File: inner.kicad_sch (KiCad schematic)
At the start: 5 parts, among them J1 FFC 10x1 0.5mm, J2 USB_A, J3 OLED, J4 Encoder

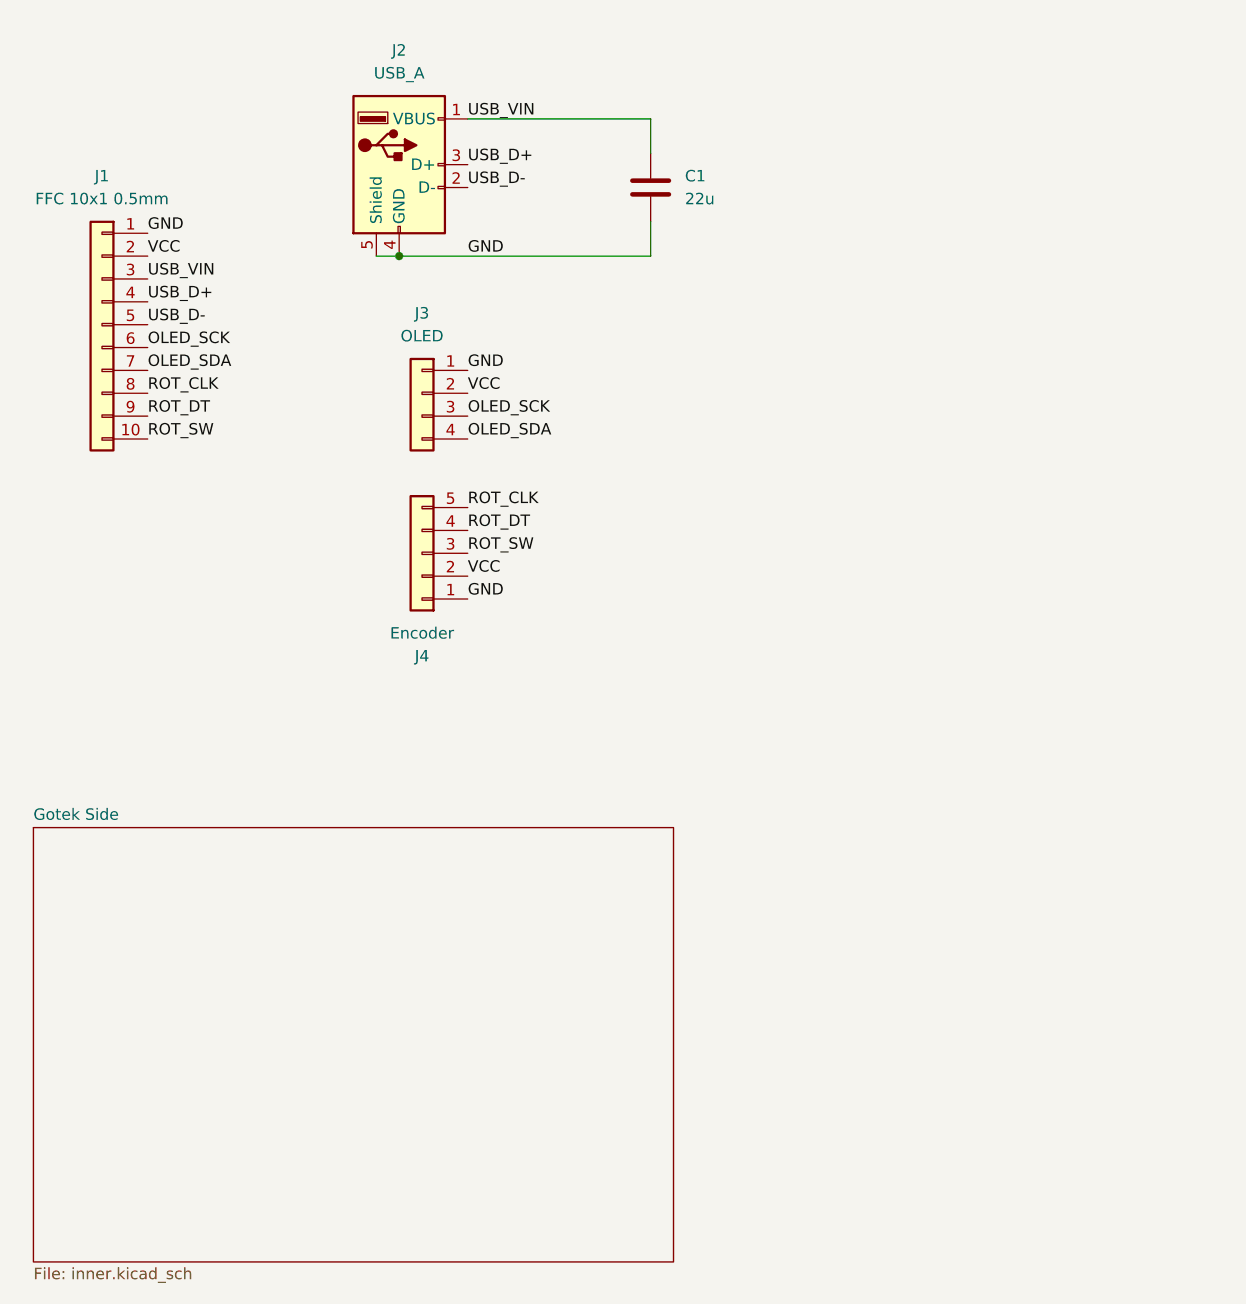
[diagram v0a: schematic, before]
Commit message: Add adapter piece, need to work out mounting
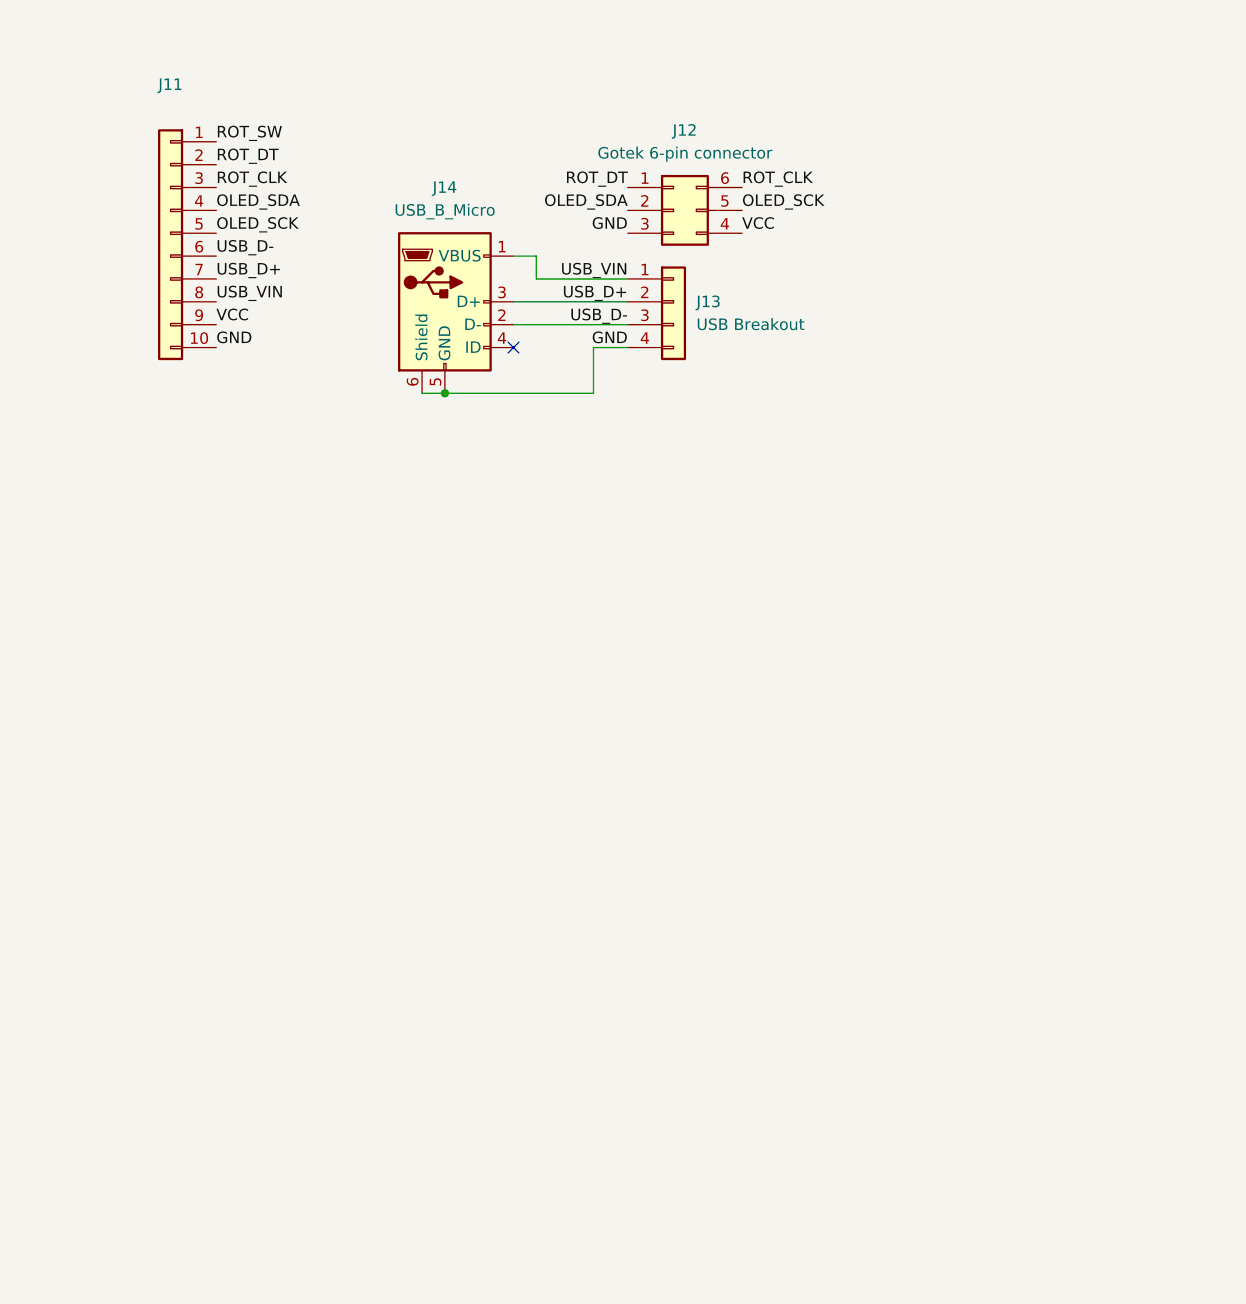
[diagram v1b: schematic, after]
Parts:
- removed C1: 22u, Capacitor_THT:CP_Radial_D5.0mm_P2.50mm, symbol Device:C
- removed J1: FFC 10x1 0.5mm, Connector_FFC-FPC:Molex_54548-1071_1x10-1MP_P0.5mm_Horizontal, symbol Connector_Generic:Conn_01x10
- removed J2: USB_A, Connector_USB:USB_A_Molex_67643_Horizontal, symbol Connector:USB_A
- removed J3: OLED, Connector_PinHeader_2.54mm:PinHeader_1x04_P2.54mm_Vertical, symbol Connector_Generic:Conn_01x04
- removed J4: Encoder, Connector_PinHeader_2.54mm:PinHeader_1x05_P2.54mm_Vertical, symbol Connector_Generic:Conn_01x05
- added J11: FFC 10x1 0.5mm, Connector_FFC-FPC:Molex_54548-1071_1x10-1MP_P0.5mm_Horizontal, symbol Connector_Generic:Conn_01x10
- added J12: Gotek 6-pin connector, Connector_PinHeader_2.54mm:PinHeader_2x03_P2.54mm_Vertical, symbol Connector_Generic:Conn_02x03_Counter_Clockwise
- added J13: USB Breakout, Connector_PinHeader_2.54mm:PinHeader_1x04_P2.54mm_Vertical, symbol Connector_Generic:Conn_01x04
- added J14: USB_B_Micro, Connector_USB:USB_Micro-B_Amphenol_10118194_Horizontal, symbol Connector:USB_B_Micro
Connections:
- net GND: now also J11.10 (Pin_10), J12.3 (Pin_3), J13.4 (Pin_4), J14.5 (GND), J14.6 (Shield)
- net OLED_SCK: now also J11.5 (Pin_5), J12.5 (Pin_5)
- net OLED_SDA: now also J11.4 (Pin_4), J12.2 (Pin_2)
- net ROT_CLK: now also J11.3 (Pin_3), J12.6 (Pin_6)
- net ROT_DT: now also J11.2 (Pin_2), J12.1 (Pin_1)
- net ROT_SW: now also J11.1 (Pin_1)
- net USB_D+: now also J11.7 (Pin_7), J13.2 (Pin_2), J14.3 (D+)
- net USB_D-: now also J11.6 (Pin_6), J13.3 (Pin_3), J14.2 (D-)
- net USB_VIN: now also J11.8 (Pin_8), J13.1 (Pin_1), J14.1 (VBUS)
- net VCC: now also J11.9 (Pin_9), J12.4 (Pin_4)
- no-connect marks 0 -> 1
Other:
- removed sheet Gotek Side

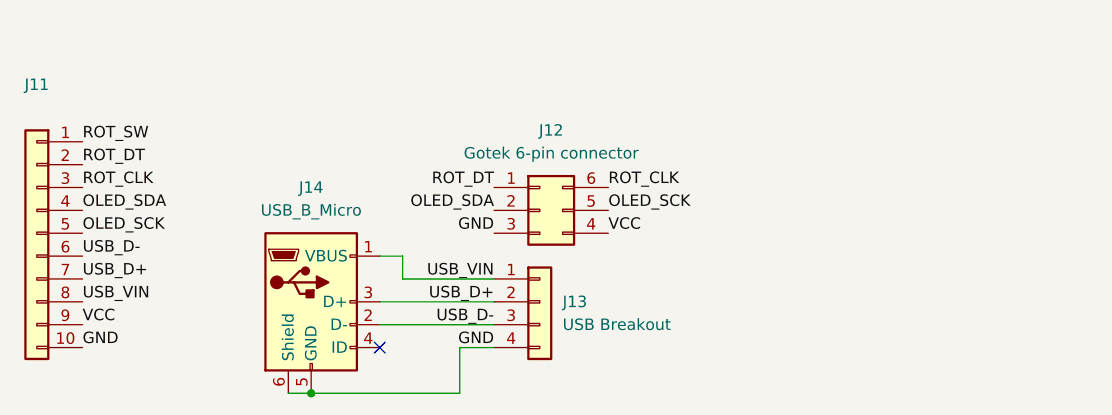
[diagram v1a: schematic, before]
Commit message: Breakout board only for newer goteks
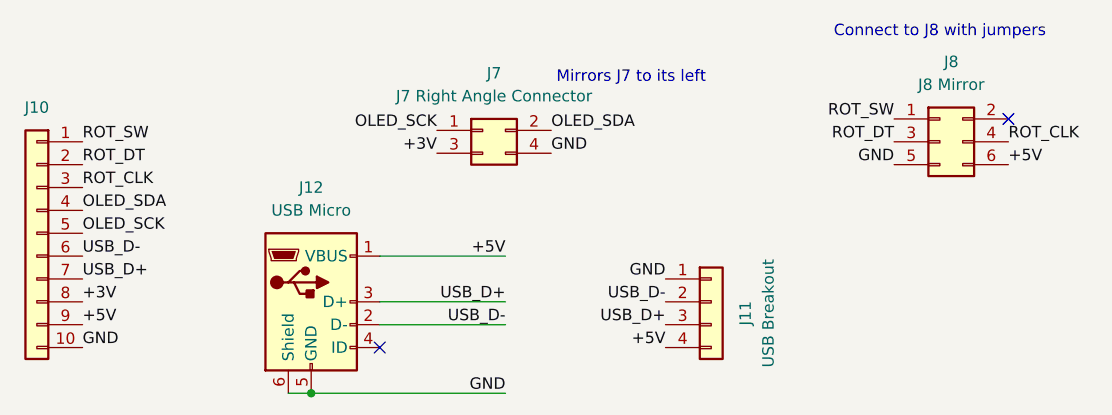
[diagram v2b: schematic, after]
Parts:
- removed J13: USB Breakout, Connector_PinHeader_2.54mm:PinHeader_1x04_P2.54mm_Vertical, symbol Connector_Generic:Conn_01x04
- added J11: USB Breakout, Connector_PinHeader_2.54mm:PinHeader_1x04_P2.54mm_Vertical, symbol Connector_Generic:Conn_01x04
- added J7: J7 Right Angle Connector, Connector_PinHeader_2.54mm:PinHeader_2x02_P2.54mm_Vertical, symbol Connector_Generic:Conn_02x02_Odd_Even
- J12: renamed from J14; value USB_B_Micro -> USB Micro
- J8: renamed from J12; value Gotek 6-pin connector -> J8 Mirror; symbol Connector_Generic:Conn_02x03_Counter_Clockwise -> Connector_Generic:Conn_02x03_Odd_Even
- renumbered J11 to J10
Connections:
- net GND: now also J8.5 (Pin_5), J11.1 (Pin_1), J7.4 (Pin_4); no longer J8.3 (Pin_3)
- net OLED_SCK: now also J7.1 (Pin_1); no longer J8.5 (Pin_5)
- net OLED_SDA: now also J7.2 (Pin_2); no longer J8.2 (Pin_2)
- net ROT_CLK: now also J8.4 (Pin_4); no longer J8.6 (Pin_6)
- net ROT_DT: now also J8.3 (Pin_3); no longer J8.1 (Pin_1)
- net ROT_SW: now also J8.1 (Pin_1)
- net USB_D+: now also J11.3 (Pin_3)
- net USB_D-: now also J11.2 (Pin_2)
- net USB_VIN renamed +3V
- net +3V: now also J7.3 (Pin_3); no longer J12.1 (VBUS)
- net VCC renamed +5V
- net +5V: now also J12.1 (VBUS), J8.6 (Pin_6), J11.4 (Pin_4); no longer J8.4 (Pin_4)
- no-connect marks 1 -> 2
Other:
- note added: "Connect to J8 with jumpers"
- note added: "Mirrors J7 to its left"
- moved on the sheet: J8

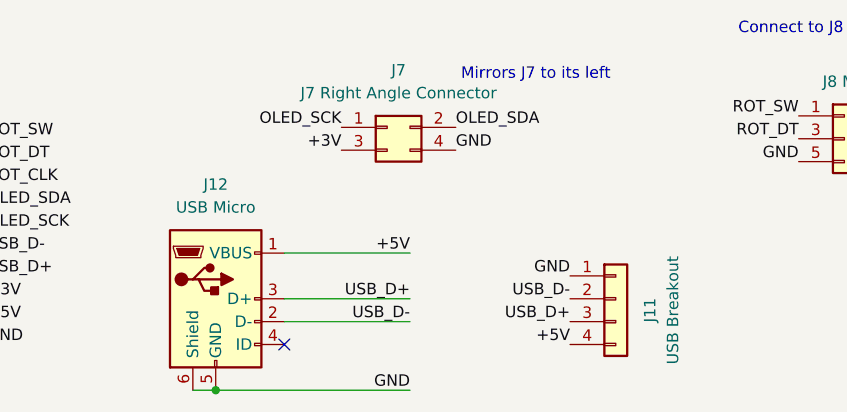
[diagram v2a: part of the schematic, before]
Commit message: Match D+/D- positions better
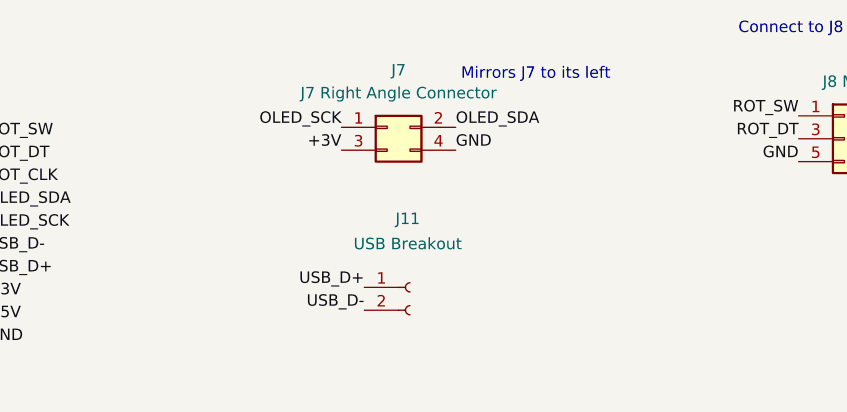
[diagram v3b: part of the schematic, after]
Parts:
- removed J12: USB Micro, Connector_USB:USB_Micro-B_Amphenol_10118194_Horizontal, symbol Connector:USB_B_Micro
- J11: footprint Connector_PinHeader_2.54mm:PinHeader_1x04_P2.54mm_Vertical -> Connector_PinHeader_2.54mm:PinHeader_1x02_P2.54mm_Vertical; symbol Connector_Generic:Conn_01x04 -> Connector:Conn_01x02_Socket
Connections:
- net +5V: no longer J11.4 (Pin_4)
- net GND: no longer J11.1 (Pin_1)
- net USB_D+: now also J11.1 (Pin_1); no longer J11.3 (Pin_3)
- no-connect marks 2 -> 1
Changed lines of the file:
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@@
 	(generator_version "8.0")
 	(paper "A4")
-	(junction
-		(at 71.12 73.66)
-		(diameter 0)
-		(color 0 0 0 0)
-	)
-	(no_connect
-		(at 78.74 68.58)
-	)
 	(no_connect
 		(at 148.59 43.18)
-	)
-	(wire
-		(pts
-			(xy 71.12 73.66) (xy 92.71 73.66)
-		)
-		(stroke
-			(width 0)
-			(type default)
-		)
-	)
-	(wire
-		(pts
-			(xy 78.74 63.5) (xy 92.71 63.5)
-		)
-		(stroke
-			(width 0)
-			(type default)
-		)
-	)
-	(wire
-		(pts
-			(xy 78.74 66.04) (xy 92.71 66.04)
-		)
-		(stroke
-			(width 0)
-			(type default)
-		)
-	)
-	(wire
-		(pts
-			(xy 68.58 73.66) (xy 71.12 73.66)
-		)
-		(stroke
-			(width 0)
-			(type default)
-		)
-	)
-	(wire
-		(pts
-			(xy 78.74 58.42) (xy 92.71 58.42)
-		)
-		(stroke
-			(width 0)
-			(type default)
-		)
 	)
 	(text "Connect to J8 with jumpers"
@@
 	)
 	(label "USB_D-"
-		(at 110.49 63.5 180)
+		(at 87.63 64.77 180)
 		(fields_autoplaced yes)
 		(effects
@@
 		)
 	)
-	(label "GND"
-		(at 110.49 60.96 180)
-		(fields_autoplaced yes)
-		(effects
-			(font
-				(size 1.27 1.27)
-			)
-			(justify right bottom)
-		)
-	)
 	(label "+5V"
 		(at 148.59 48.26 0)
@@
 	)
 	(label "USB_D+"
-		(at 110.49 66.04 180)
+		(at 87.63 62.23 180)
 		(fields_autoplaced yes)
 		(effects
@@
 		)
 	)
-	(label "USB_D+"
-		(at 92.71 63.5 180)
-		(fields_autoplaced yes)
-		(effects
-			(font
-				(size 1.27 1.27)
-			)
-			(justify right bottom)
-		)
-	)
 	(label "ROT_SW"
 		(at 45.72 45.72 0)
@@
 		)
 	)
-	(label "USB_D-"
-		(at 92.71 66.04 180)
-		(fields_autoplaced yes)
-		(effects
-			(font
-				(size 1.27 1.27)
-			)
-			(justify right bottom)
-		)
-	)
-	(label "+5V"
-		(at 110.49 68.58 180)
-		(fields_autoplaced yes)
-		(effects
-			(font
-				(size 1.27 1.27)
-			)
-			(justify right bottom)
-		)
-	)
 	(label "ROT_SW"
 		(at 135.89 43.18 180)
@@
 			)
 			(justify left bottom)
-		)
-	)
-	(label "GND"
-		(at 92.71 73.66 180)
-		(fields_autoplaced yes)
-		(effects
-			(font
-				(size 1.27 1.27)
-			)
-			(justify right bottom)
-		)
-	)
-	(label "+5V"
-		(at 92.71 58.42 180)
-		(fields_autoplaced yes)
-		(effects
-			(font
-				(size 1.27 1.27)
-			)
-			(justify right bottom)
 		)
 	)
@@
 				(path "/b341c288-9908-489c-8721-82a569e81f5e/2f858839-97ab-4505-8bc1-6a432d3cea76"
 					(reference "J7")
-					(unit 1)
-				)
-			)
-		)
-	)
-	(symbol
-		(lib_id "Connector:USB_B_Micro")
-		(at 71.12 63.5 0)
-		(unit 1)
-		(exclude_from_sim no)
-		(in_bom yes)
-		(on_board yes)
-		(dnp no)
-		(fields_autoplaced yes)
-		(property "Reference" "J12"
-			(at 71.12 50.8 0)
-			(effects
-				(font
-					(size 1.27 1.27)
-				)
-			)
-		)
-		(property "Value" "USB Micro"
-			(at 71.12 53.34 0)
-			(effects
-				(font
-					(size 1.27 1.27)
-				)
-			)
-		)
-		(property "Footprint" "Connector_USB:USB_Micro-B_Amphenol_10118194_Horizontal"
-			(at 74.93 64.77 0)
-			(effects
-				(font
-					(size 1.27 1.27)
-				)
-				(hide yes)
-			)
-		)
-		(property "Datasheet" "~"
-			(at 74.93 64.77 0)
-			(effects
-				(font
-					(size 1.27 1.27)
-				)
-				(hide yes)
-			)
-		)
-		(property "Description" "USB Micro Type B connector"
-			(at 71.12 63.5 0)
-			(effects
-				(font
-					(size 1.27 1.27)
-				)
-				(hide yes)
-			)
-		)
-		(property "Notes" ""
-			(at 71.12 63.5 0)
-			(effects
-				(font
-					(size 1.27 1.27)
-				)
-			)
-		)
-		(pin "5"
-		)
-		(pin "6"
-		)
-		(pin "2"
-		)
-		(pin "4"
-		)
-		(pin "3"
-		)
-		(pin "1"
-		)
-		(instances
-			(project "gotek-breakout"
-				(path "/b341c288-9908-489c-8721-82a569e81f5e/2f858839-97ab-4505-8bc1-6a432d3cea76"
-					(reference "J12")
 					(unit 1)
 				)
@@
 	)
 	(symbol
-		(lib_id "Connector_Generic:Conn_01x04")
-		(at 115.57 63.5 0)
+		(lib_id "Connector:Conn_01x02_Socket")
+		(at 92.71 62.23 0)
 		(unit 1)
 		(exclude_from_sim no)
@@
 		(dnp no)
 		(property "Reference" "J11"
-			(at 119.38 64.77 90)
+			(at 92.456 54.61 0)
 			(effects
 				(font
@@
 		)
 		(property "Value" "USB Breakout"
-			(at 121.92 64.77 90)
-			(effects
-				(font
-					(size 1.27 1.27)
-				)
-			)
-		)
-		(property "Footprint" "Connector_PinHeader_2.54mm:PinHeader_1x04_P2.54mm_Vertical"
-			(at 115.57 63.5 0)
+			(at 92.456 57.404 0)
+			(effects
+				(font
+					(size 1.27 1.27)
+				)
+			)
+		)
+		(property "Footprint" "Connector_PinHeader_2.54mm:PinHeader_1x02_P2.54mm_Vertical"
+			(at 92.71 62.23 0)
 			(effects
 				(font
@@
 		)
 		(property "Datasheet" "~"
-			(at 115.57 63.5 0)
-			(effects
-				(font
-					(size 1.27 1.27)
-				)
-				(hide yes)
-			)
-		)
-		(property "Description" ""
-			(at 115.57 63.5 0)
+			(at 92.71 62.23 0)
+			(effects
+				(font
+					(size 1.27 1.27)
+				)
+				(hide yes)
+			)
+		)
+		(property "Description" "Generic connector, single row, 01x02, script generated"
+			(at 92.71 62.23 0)
 			(effects
 				(font
@@
 		)
 		(property "Notes" ""
-			(at 115.57 63.5 0)
+			(at 92.71 62.23 0)
 			(effects
 				(font
@@
 		(pin "1"
 		)
-		(pin "3"
-		)
-		(pin "4"
-		)
 		(pin "2"
